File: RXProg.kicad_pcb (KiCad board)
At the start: 2 copper layers, 5 parts, among them J1 DIP-28, U1 STM32G474CETx, U2 SN74ALVC164245DL, U3 LSF0108BQ, U4 MIC5317-3.3xM5

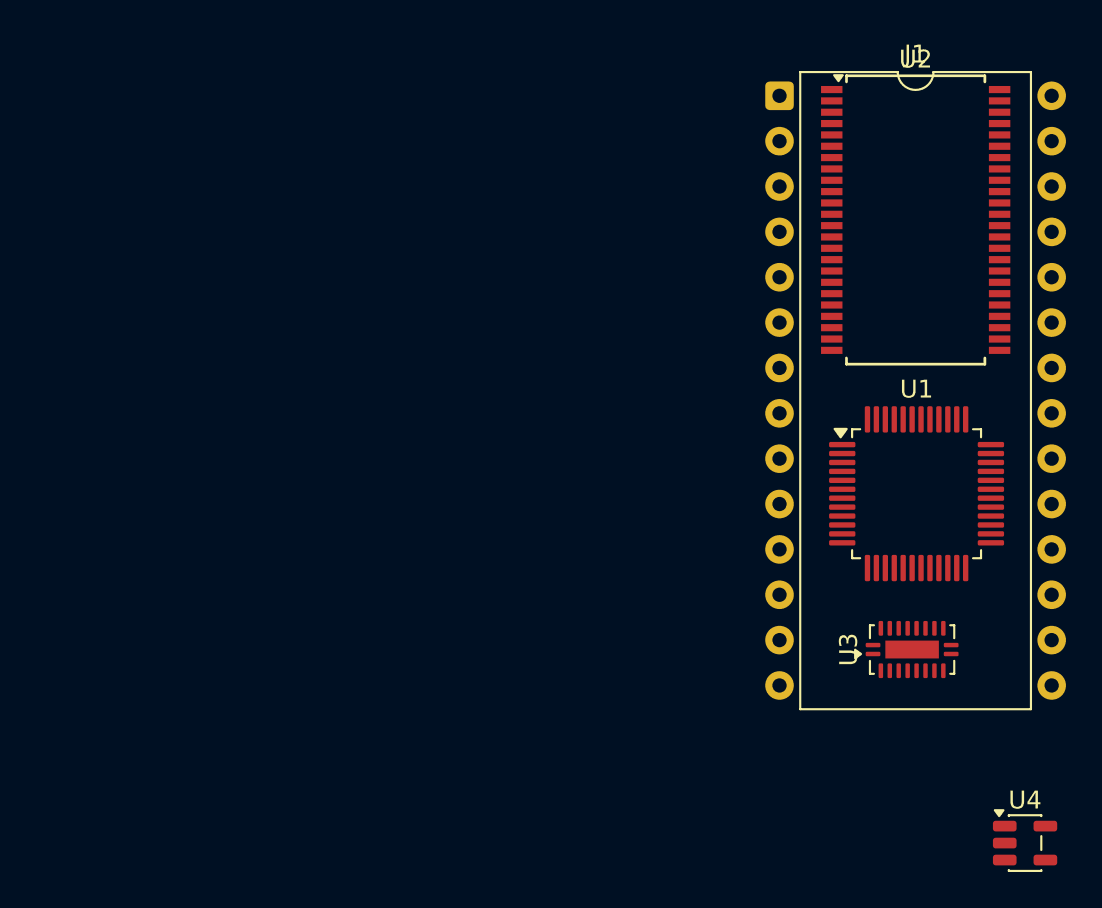
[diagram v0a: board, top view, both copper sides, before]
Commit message: Add level shifters
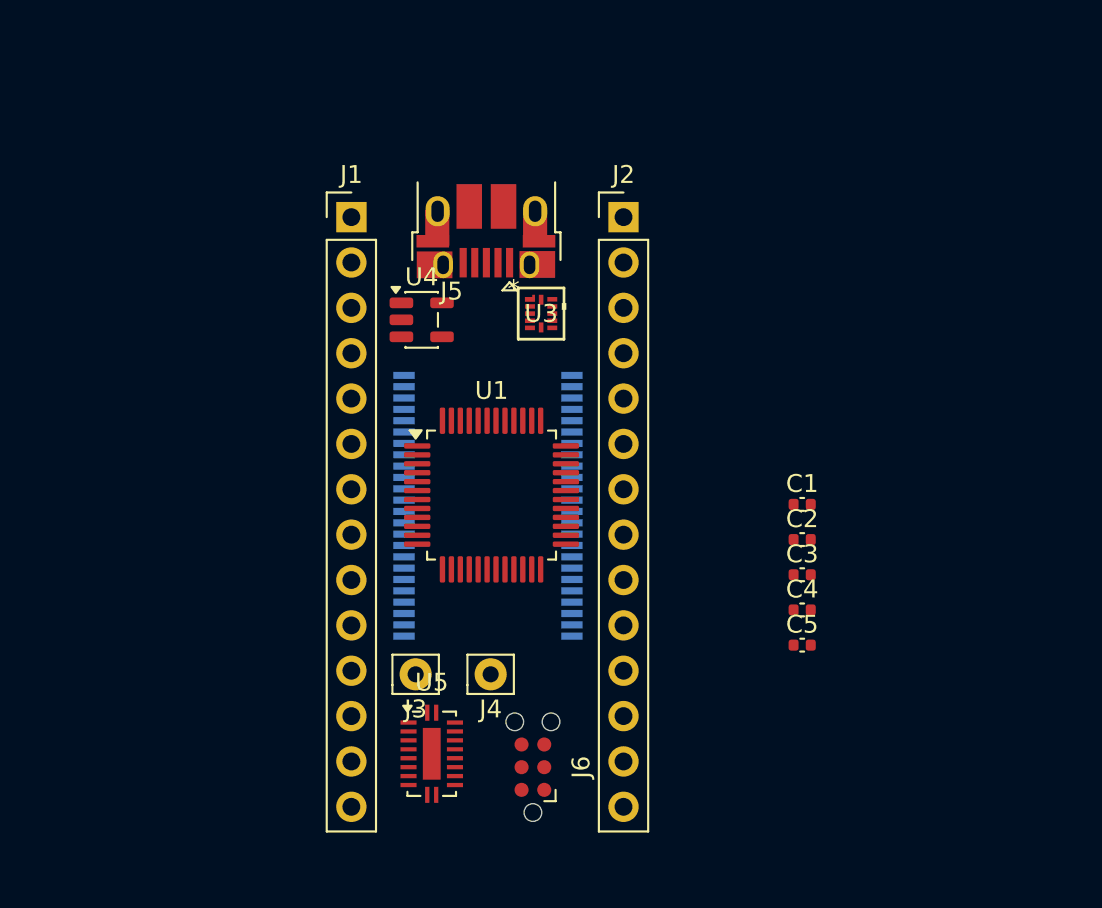
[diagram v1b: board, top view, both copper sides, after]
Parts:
- added C1: 100n, Capacitor_SMD:C_0402_1005Metric, F.Cu at (143.8, 107.7)
- added C2: 100n, Capacitor_SMD:C_0402_1005Metric, F.Cu at (143.8, 109.7)
- added C3: 100n, Capacitor_SMD:C_0402_1005Metric, F.Cu at (143.8, 111.6)
- added C4: 100n, Capacitor_SMD:C_0402_1005Metric, F.Cu at (143.8, 113.6)
- added C5: 100n, Capacitor_SMD:C_0402_1005Metric, F.Cu at (143.8, 115.6)
- added J2: Conn_01x14, Connector_PinHeader_2.54mm:PinHeader_1x14_P2.54mm_Vertical, F.Cu at (133.8, 91.6)
- added J3: Pin, Connector_Pin:Pin_D0.9mm_L10.0mm_W2.4mm_FlatFork, F.Cu at (122.2, 117.2)
- added J4: Pin, Connector_Pin:Pin_D0.9mm_L10.0mm_W2.4mm_FlatFork, F.Cu at (126.4, 117.2)
- added J5: USB_B_Micro, Connector_USB:USB_Micro-B_Amphenol_10103594-0001LF_Horizontal, F.Cu at (126.1, 92.4)
- added J6: Conn_ARM_SWD_TagConnect_TC2030-NL, Connector:Tag-Connect_TC2030-IDC-NL_2x03_P1.27mm_Vertical, F.Cu at (128.8, 122.4)
- added U5: FXMA108, Package_DFN_QFN:WQFN-20-1EP_2.5x4.5mm_P0.5mm_EP1x2.9mm, F.Cu at (123.1, 121.7)
- J1: value DIP-28 -> Conn_01x14; footprint Package_DIP:DIP-28_W15.24mm -> Connector_PinHeader_2.54mm:PinHeader_1x14_P2.54mm_Vertical
- U2: moved to B.Cu
- U3: value LSF0108BQ -> TXU0104RUTR; footprint Package_DFN_QFN:DHVQFN-20-1EP_2.5x4.5mm_P0.5mm_EP1x3mm -> footprints:QFN_04RUTR_TEX
- moved U4 44.7 mm to (122.5, 97.3)
- moved U2 28.8 mm to (126.2, 107.8), turned to 180 degrees
- moved U3 28.0 mm to (129.2, 97.0), turned to 0 degrees
- moved J1 24.9 mm to (118.6, 91.6)
- moved U1 23.8 mm to (126.5, 107.2)
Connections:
- U1 pad 1: unconnected-(U1-VBAT-Pad1) -> +3V3
- U1 pad 10: unconnected-(U1-PA2-Pad10) -> Net-(U1-PA2)
- U1 pad 11: unconnected-(U1-PA3-Pad11) -> Net-(U1-PA3)
- U1 pad 12: unconnected-(U1-PA4-Pad12) -> Net-(U1-PA4)
- U1 pad 13: unconnected-(U1-PA5-Pad13) -> Net-(U1-PA5)
- U1 pad 14: unconnected-(U1-PA6-Pad14) -> Net-(U1-PA6)
- U1 pad 15: unconnected-(U1-PA7-Pad15) -> Net-(U1-PA7)
- U1 pad 16: A0 -> Net-(U1-PB0)
- U1 pad 17: A1 -> Net-(U1-PB1)
- U1 pad 18: A2 -> Net-(U1-PB2)
- U1 pad 19: unconnected-(U1-VSSA-Pad19) -> GND
- U1 pad 2: unconnected-(U1-PC13-Pad2) -> Net-(U1-PC13)
- U1 pad 20: unconnected-(U1-VREF+-Pad20) -> +3V3
- U1 pad 21: unconnected-(U1-VDDA-Pad21) -> +3V3
- U1 pad 22: A10 -> Net-(U1-PB10)
- U1 pad 23: Net-(U1-VSS-Pad23) -> GND
- U1 pad 24: unconnected-(U1-VDD-Pad24) -> +3V3
- U1 pad 25: ~{WE}/A11 -> Net-(U1-PB11)
- U1 pad 26: /A12 -> Net-(U1-PB12)
- U1 pad 27: unconnected-(U1-PB13-Pad27) -> Net-(U1-PB13)
- U1 pad 28: unconnected-(U1-PB14-Pad28) -> Net-(U1-PB14)
- U1 pad 29: unconnected-(U1-PB15-Pad29) -> Net-(U1-PB15)
- U1 pad 3: unconnected-(U1-PC14-Pad3) -> Net-(U1-PC14)
- U1 pad 30: unconnected-(U1-PA8-Pad30) -> Net-(U1-PA8)
- U1 pad 31: unconnected-(U1-PA9-Pad31) -> ~{ADDR_OE}
- U1 pad 33: unconnected-(U1-PA11-Pad33) -> Net-(J5-D-)
- U1 pad 34: unconnected-(U1-PA12-Pad34) -> Net-(J5-D+)
- U1 pad 35: Net-(U1-VSS-Pad23) -> GND
- U1 pad 36: unconnected-(U1-VDD-Pad36) -> +3V3
- U1 pad 4: unconnected-(U1-PC15-Pad4) -> Net-(U1-PC15)
- U1 pad 40: A3 -> Net-(U1-PB3)
- U1 pad 41: A4 -> Net-(U1-PB4)
- U1 pad 42: A5 -> Net-(U1-PB5)
- U1 pad 43: A6 -> Net-(U1-PB6)
- U1 pad 44: A7 -> Net-(U1-PB7)
- U1 pad 45: A8 -> Net-(U1-PB8)
- U1 pad 46: A9 -> Net-(U1-PB9)
- U1 pad 47: Net-(U1-VSS-Pad23) -> GND
- U1 pad 48: unconnected-(U1-VDD-Pad48) -> +3V3
- U1 pad 8: unconnected-(U1-PA0-Pad8) -> Net-(U1-PA0)
- U1 pad 9: unconnected-(U1-PA1-Pad9) -> Net-(U1-PA1)
- U2 pad 1: unconnected-(U2-1DIR-Pad1) -> GND
- U2 pad 10: Net-(U2-GND-Pad10) -> GND
- U2 pad 11: unconnected-(U2-1B6-Pad11) -> A6
- U2 pad 12: unconnected-(U2-1B7-Pad12) -> A7
- U2 pad 13: unconnected-(U2-2B0-Pad13) -> A8
- U2 pad 14: unconnected-(U2-2B1-Pad14) -> A9
- U2 pad 15: Net-(U2-GND-Pad10) -> GND
- U2 pad 16: unconnected-(U2-2B2-Pad16) -> A10
- U2 pad 17: unconnected-(U2-2B3-Pad17) -> ~{WE}/A11
- U2 pad 18: Net-(U2-V_{CC(B)}-Pad18) -> /VBAT
- U2 pad 19: unconnected-(U2-2B4-Pad19) -> /A12
- U2 pad 2: unconnected-(U2-1B0-Pad2) -> A0
- U2 pad 20: unconnected-(U2-2B5-Pad20) -> ~{CS1}
- U2 pad 21: Net-(U2-GND-Pad10) -> GND
- U2 pad 22: unconnected-(U2-2B6-Pad22) -> ~{CS2}
- U2 pad 23: unconnected-(U2-2B7-Pad23) -> ~{CS3}
- U2 pad 24: unconnected-(U2-2DIR-Pad24) -> GND
- U2 pad 25: unconnected-(U2-2~{OE}-Pad25) -> ~{ADDR_OE}
- U2 pad 26: unconnected-(U2-2A7-Pad26) -> Net-(U1-PB15)
- U2 pad 27: unconnected-(U2-2A6-Pad27) -> Net-(U1-PB14)
- U2 pad 28: Net-(U2-GND-Pad10) -> GND
- U2 pad 29: unconnected-(U2-2A5-Pad29) -> Net-(U1-PB13)
- U2 pad 3: unconnected-(U2-1B1-Pad3) -> A1
- U2 pad 30: unconnected-(U2-2A4-Pad30) -> Net-(U1-PB12)
- U2 pad 31: Net-(U2-V_{CC(A)}-Pad31) -> +3V3
- U2 pad 32: unconnected-(U2-2A3-Pad32) -> Net-(U1-PB11)
- U2 pad 33: unconnected-(U2-2A2-Pad33) -> Net-(U1-PB10)
- U2 pad 34: Net-(U2-GND-Pad10) -> GND
- U2 pad 35: unconnected-(U2-2A1-Pad35) -> Net-(U1-PB9)
- U2 pad 36: unconnected-(U2-2A0-Pad36) -> Net-(U1-PB8)
- U2 pad 37: unconnected-(U2-1A7-Pad37) -> Net-(U1-PB7)
- U2 pad 38: unconnected-(U2-1A6-Pad38) -> Net-(U1-PB6)
- U2 pad 39: Net-(U2-GND-Pad10) -> GND
- U2 pad 4: Net-(U2-GND-Pad10) -> GND
- U2 pad 40: unconnected-(U2-1A5-Pad40) -> Net-(U1-PB5)
- U2 pad 41: unconnected-(U2-1A4-Pad41) -> Net-(U1-PB4)
- U2 pad 42: Net-(U2-V_{CC(A)}-Pad31) -> +3V3
- U2 pad 43: unconnected-(U2-1A3-Pad43) -> Net-(U1-PB3)
- U2 pad 44: unconnected-(U2-1A2-Pad44) -> Net-(U1-PB2)
- U2 pad 45: Net-(U2-GND-Pad10) -> GND
- U2 pad 46: unconnected-(U2-1A1-Pad46) -> Net-(U1-PB1)
- U2 pad 47: unconnected-(U2-1A0-Pad47) -> Net-(U1-PB0)
- U2 pad 48: unconnected-(U2-1~{OE}-Pad48) -> ~{ADDR_OE}
- U2 pad 5: unconnected-(U2-1B2-Pad5) -> A2
- U2 pad 6: unconnected-(U2-1B3-Pad6) -> A3
- U2 pad 7: Net-(U2-V_{CC(B)}-Pad18) -> /VBAT
- U2 pad 8: unconnected-(U2-1B4-Pad8) -> A4
- U2 pad 9: unconnected-(U2-1B5-Pad9) -> A5
- U3 pad 1: unconnected-(U3-GND-Pad1) -> /VBAT
- U3 pad 10: unconnected-(U3-A8-Pad10) -> Net-(U1-PC13)
- U3 pad 11: unconnected-(U3-B8-Pad11) -> +3V3
- U3 pad 12: unconnected-(U3-B7-Pad12) -> +3V3
- U3 pad 2: unconnected-(U3-RefA-Pad2) -> VBAT/~{RES}
- U3 pad 3: unconnected-(U3-A1-Pad3) -> RES/~{OE}
- U3 pad 4: unconnected-(U3-A2-Pad4) -> /~{WE}
- U3 pad 6: unconnected-(U3-A4-Pad6) -> GND
- U3 pad 8: unconnected-(U3-A6-Pad8) -> Net-(U1-PC15)
- U3 pad 9: unconnected-(U3-A7-Pad9) -> Net-(U1-PC14)
- U4 pad 1: unconnected-(U4-VIN-Pad1) -> /VBAT
- U4 pad 2: unconnected-(U4-GND-Pad2) -> GND
- U4 pad 3: unconnected-(U4-EN-Pad3) -> /VBAT
- U4 pad 5: unconnected-(U4-VOUT-Pad5) -> +3V3

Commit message: Add
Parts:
- added C6: 100n, Capacitor_SMD:C_0402_1005Metric, F.Cu at (144.2, 119.5)
- added C7: 10u, Capacitor_SMD:C_0402_1005Metric, F.Cu at (144.2, 121.5)
- added C8: 10u, Capacitor_SMD:C_0402_1005Metric, F.Cu at (144.2, 123.4)
- added D1: CD214A-B140LR, footprints:CD214A, F.Cu at (126.2, 98.5)
- added U6: FM25V02A, footprints:DFN-8_4x4.5mm_P0.95mm, B.Cu at (123.2, 121.8)
- J6: value Conn_ARM_SWD_TagConnect_TC2030-NL -> SWD
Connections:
- J6 pad 1: unconnected-(J6-VCC-Pad1) -> +3V3
- J6 pad 2: unconnected-(J6-SWDIO-Pad2) -> Net-(J6-SWDIO)
- J6 pad 3: unconnected-(J6-~{RESET}-Pad3) -> ~{NRST}
- J6 pad 4: unconnected-(J6-SWCLK-Pad4) -> Net-(J6-SWCLK)
- J6 pad 5: unconnected-(J6-GND-Pad5) -> GND
- U1 pad 32: unconnected-(U1-PA10-Pad32) -> ~{FRAM_CS}
- U1 pad 37: unconnected-(U1-PA13-Pad37) -> Net-(J6-SWDIO)
- U1 pad 38: unconnected-(U1-PA14-Pad38) -> Net-(J6-SWCLK)
- U1 pad 7: unconnected-(U1-PG10-Pad7) -> ~{NRST}

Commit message: Start routing
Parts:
- removed U6: FM25V02A, footprints:DFN-8_4x4.5mm_P0.95mm
- added C10: 100n, Capacitor_SMD:C_0201_0603Metric, F.Cu at (147.7, 114.8)
- added C11: 100n, Capacitor_SMD:C_0201_0603Metric, F.Cu at (147.7, 116.8)
- added C9: 100n, Capacitor_SMD:C_0201_0603Metric, F.Cu at (126.8, 96.7)
- added JP1: RX5_Select, Jumper:SolderJumper-2_P1.3mm_Open_RoundedPad1.0x1.5mm, F.Cu at (107.1, 99.3)
- C1, C2, C3, C4, C5, C6: footprint Capacitor_SMD:C_0402_1005Metric -> Capacitor_SMD:C_0201_0603Metric
- C7: value 10u -> 1u; footprint Capacitor_SMD:C_0402_1005Metric -> Capacitor_SMD:C_0201_0603Metric; moved to B.Cu
- C8: value 10u -> 1u; footprint Capacitor_SMD:C_0402_1005Metric -> Capacitor_SMD:C_0201_0603Metric
- D1: value CD214A-B140LR -> RB531SM-30T2R; footprint footprints:CD214A -> Diode_SMD:D_SOD-523
- J3, J4: footprint Connector_Pin:Pin_D0.9mm_L10.0mm_W2.4mm_FlatFork -> footprints:Pin
- moved C8 35.4 mm to (127.2, 92.4), turned to 90 degrees
- moved C7 31.6 mm to (131.2, 92.6), turned to 90 degrees
- moved J5 31.1 mm to (126.2, 123.5), turned to 0 degrees
- moved J6 27.0 mm to (102.4, 116.3)
- moved C6 26.8 mm to (129.0, 97.4), turned to 180 degrees
- moved U5 14.6 mm to (109.0, 125.1)
- moved J3 12.9 mm to (109.8, 113.8)
- moved J4 12.9 mm to (114.0, 113.8)
- moved U4 9.14 mm to (129.8, 91.8), turned to 180 degrees
- moved D1 4.97 mm to (130.8, 96.5)
- moved U3 1.71 mm to (128.6, 95.4), turned to 180 degrees
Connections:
- net Net-(J5-D+) renamed /D_+
- net Net-(J5-D-) renamed /D_-
- C6 pad 1: +3V3 -> /VBAT
- U1 pad 39: unconnected-(U1-PA15-Pad39) -> Net-(JP1-B)
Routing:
- net RES/~{OE}: track 0.00 -> 14.7 mm, vias 0 -> 1
- net /VBAT: track 0.00 -> 7.98 mm, vias 0 -> 2
- net GND: track 0.00 -> 5.77 mm, vias 0 -> 4
- net VBAT/~{RES}: track 0.00 -> 4.95 mm
- net /~{WE}: track 0.00 -> 4.95 mm
- net +3V3: track 0.00 -> 1.87 mm
- added copper zone on F.Cu, net +3V3
- added copper zone on In1.Cu, net GND
- added copper zone on In2.Cu, net GND
- added copper zone on B.Cu, net /VBAT
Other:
- board outline added: 18.8 x 36.6 mm
- copper layers 2 -> 4

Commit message: Continue
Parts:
- moved J6 30.1 mm to (122.6, 94.0), turned to -90 degrees
- moved JP1 19.6 mm to (126.0, 94.2), turned to -90 degrees
- moved C8 0.66 mm to (127.2, 91.7), turned to -90 degrees
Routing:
- net GND: track 5.77 -> 8.75 mm, vias 4 -> 5
- net /VBAT: track 7.98 -> 8.80 mm, vias 2 -> 3
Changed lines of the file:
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@@
 		(capping no)
 		(filling no)
-		(zone_defaults)
 		(pcbplotparams
 			(layerselection 0x00000000_00000000_55555555_5755f5ff)
@@
 	(footprint "Connector:Tag-Connect_TC2030-IDC-NL_2x03_P1.27mm_Vertical"
 		(layer "F.Cu")
-		(at 102.435 116.33 90)
+		(at 122.615 93.98 -90)
 		(descr "Tag-Connect programming header; http://www.tag-connect.com/Materials/TC2030-IDC-NL.pdf")
 		(tags "tag connect programming header pogo pins")
@@
 		)
 		(property "Datasheet" "https://www.tag-connect.com/wp-content/uploads/bsk-pdf-manager/TC2030-CTX_1.pdf"
-			(at 0 0 90)
+			(at 0 0 270)
 			(unlocked yes)
 			(layer "F.Fab")
@@
 		)
 		(property "Description" "Tag-Connect ARM Cortex SWD JTAG connector, 6 pin, no legs"
-			(at 0 0 90)
+			(at 0 0 270)
 			(unlocked yes)
 			(layer "F.Fab")
@@
 		(duplicate_pad_numbers_are_jumpers no)
 		(fp_line
-			(start -1.27 1.27)
-			(end -1.905 1.27)
+			(start -1.905 1.27)
+			(end -1.905 0.635)
 			(stroke
 				(width 0.12)
@@
 		)
 		(fp_line
-			(start -1.905 1.27)
-			(end -1.905 0.635)
+			(start -1.27 1.27)
+			(end -1.905 1.27)
 			(stroke
 				(width 0.12)
@@
 		)
 		(fp_line
-			(start 3.5 -2)
-			(end 3.5 2)
+			(start -3.5 2)
+			(end -3.5 -2)
 			(stroke
 				(width 0.05)
@@
 		)
 		(fp_line
-			(start -3.5 -2)
-			(end 3.5 -2)
+			(start 3.5 2)
+			(end -3.5 2)
 			(stroke
 				(width 0.05)
@@
 		)
 		(fp_line
-			(start 3.5 2)
-			(end -3.5 2)
+			(start -3.5 -2)
+			(end 3.5 -2)
 			(stroke
 				(width 0.05)
@@
 		)
 		(fp_line
-			(start -3.5 2)
-			(end -3.5 -2)
+			(start 3.5 -2)
+			(end 3.5 2)
 			(stroke
 				(width 0.05)
@@
 		)
 		(pad "" np_thru_hole circle
-			(at -2.54 0 90)
+			(at -2.54 0 270)
 			(size 0.9906 0.9906)
 			(drill 0.9906)
@@
 		)
 		(pad "" np_thru_hole circle
-			(at 2.54 -1.016 90)
+			(at 2.54 -1.016 270)
 			(size 0.9906 0.9906)
 			(drill 0.9906)
@@
 		)
 		(pad "" np_thru_hole circle
-			(at 2.54 1.016 90)
+			(at 2.54 1.016 270)
 			(size 0.9906 0.9906)
 			(drill 0.9906)
@@
 		)
 		(pad "1" connect circle
-			(at -1.27 0.635 90)
+			(at -1.27 0.635 270)
 			(size 0.7874 0.7874)
 			(layers "F.Cu" "F.Mask")
@@
 		)
 		(pad "2" connect circle
-			(at -1.27 -0.635 90)
+			(at -1.27 -0.635 270)
 			(size 0.7874 0.7874)
 			(layers "F.Cu" "F.Mask")
@@
 		)
 		(pad "3" connect circle
-			(at 0 0.635 90)
+			(at 0 0.635 270)
 			(size 0.7874 0.7874)
 			(layers "F.Cu" "F.Mask")
@@
 		)
 		(pad "4" connect circle
-			(at 0 -0.635 90)
+			(at 0 -0.635 270)
 			(size 0.7874 0.7874)
 			(layers "F.Cu" "F.Mask")
@@
 		)
 		(pad "5" connect circle
-			(at 1.27 0.635 90)
+			(at 1.27 0.635 270)
 			(size 0.7874 0.7874)
 			(layers "F.Cu" "F.Mask")
@@
 		)
 		(pad "6" connect circle
-			(at 1.27 -0.635 90)
+			(at 1.27 -0.635 270)
 			(size 0.7874 0.7874)
 			(layers "F.Cu" "F.Mask")
@@
 			(polygon
 				(pts
-					(xy 101.8 115.06) (xy 101.8 117.6) (xy 103.07 117.6) (xy 103.07 115.06)
+					(xy 123.25 95.25) (xy 123.25 92.71) (xy 121.98 92.71) (xy 121.98 95.25)
 				)
 			)
@@
 	(footprint "Jumper:SolderJumper-2_P1.3mm_Open_RoundedPad1.0x1.5mm"
 		(layer "F.Cu")
-		(at 107.075 99.275)
+		(at 126 94.2 -90)
 		(descr "SMD Solder Jumper, 1x1.5mm, rounded Pads, 0.3mm gap, open")
 		(tags "solder jumper open")
 		(property "Reference" "JP1"
-			(at 0 -1.8 0)
+			(at 0 -1.8 90)
 			(layer "F.SilkS")
+			(hide yes)
 			(effects
 				(font
@@
 		)
 		(property "Value" "RX5_Select"
-			(at 0 1.9 0)
+			(at 0 1.9 90)
 			(layer "F.Fab")
+			(hide yes)
 			(effects
 				(font
@@
 		)
 		(property "Datasheet" ""
-			(at 0 0 0)
+			(at 0 0 270)
 			(unlocked yes)
 			(layer "F.Fab")
@@
 		)
 		(property "Description" "Solder Jumper, 2-pole, open"
-			(at 0 0 0)
+			(at 0 0 270)
 			(unlocked yes)
 			(layer "F.Fab")
@@
 		)
 		(fp_line
-			(start -1.4 0.3)
-			(end -1.4 -0.3)
+			(start 0.7 1)
+			(end -0.7 1)
 			(stroke
 				(width 0.12)
@@
 		)
 		(fp_line
-			(start -0.7 -1)
-			(end 0.7 -1)
+			(start -1.4 0.3)
+			(end -1.4 -0.3)
 			(stroke
 				(width 0.12)
@@
 		)
 		(fp_line
-			(start 0.7 1)
-			(end -0.7 1)
+			(start 1.4 -0.3)
+			(end 1.4 0.3)
 			(stroke
 				(width 0.12)
@@
 		)
 		(fp_line
-			(start 1.4 -0.3)
-			(end 1.4 0.3)
+			(start -0.7 -1)
+			(end 0.7 -1)
 			(stroke
 				(width 0.12)
@@
 		)
 		(fp_arc
-			(start -1.4 -0.3)
-			(mid -1.194975 -0.794975)
-			(end -0.7 -1)
+			(start -0.7 1)
+			(mid -1.194975 0.794975)
+			(end -1.4 0.3)
 			(stroke
 				(width 0.12)
@@
 		)
 		(fp_arc
-			(start -0.7 1)
-			(mid -1.194975 0.794975)
-			(end -1.4 0.3)
+			(start 1.4 0.3)
+			(mid 1.194975 0.794975)
+			(end 0.7 1)
 			(stroke
 				(width 0.12)
@@
 		)
 		(fp_arc
-			(start 0.7 -1)
-			(mid 1.194975 -0.794975)
-			(end 1.4 -0.3)
+			(start -1.4 -0.3)
+			(mid -1.194975 -0.794975)
+			(end -0.7 -1)
 			(stroke
 				(width 0.12)
@@
 		)
 		(fp_arc
-			(start 1.4 0.3)
-			(mid 1.194975 0.794975)
-			(end 0.7 1)
+			(start 0.7 -1)
+			(mid 1.194975 -0.794975)
+			(end 1.4 -0.3)
 			(stroke
 				(width 0.12)
@@
 		)
 		(fp_line
-			(start -1.65 -1.25)
+			(start 1.65 1.25)
 			(end -1.65 1.25)
 			(stroke
@@
 		)
 		(fp_line
-			(start -1.65 -1.25)
+			(start 1.65 1.25)
 			(end 1.65 -1.25)
 			(stroke
@@
 		)
 		(fp_line
-			(start 1.65 1.25)
+			(start -1.65 -1.25)
 			(end -1.65 1.25)
 			(stroke
@@
 		)
 		(fp_line
-			(start 1.65 1.25)
+			(start -1.65 -1.25)
 			(end 1.65 -1.25)
 			(stroke
@@
 		)
 		(pad "1" smd custom
-			(at -0.65 0)
+			(at -0.65 0 270)
 			(size 1 0.5)
 			(layers "F.Cu" "F.Mask")
@@
 		)
 		(pad "2" smd custom
-			(at 0.65 0)
+			(at 0.65 0 270)
 			(size 1 0.5)
 			(layers "F.Cu" "F.Mask")
@@
 	(footprint "Capacitor_SMD:C_0201_0603Metric"
 		(layer "F.Cu")
-		(at 127.2 92.4 90)
+		(at 127.2 91.745 -90)
 		(descr "Capacitor SMD 0201 (0603 Metric), square (rectangular) end terminal, IPC-7351 nominal, (Body size source: https://www.vishay.com/docs/20052/crcw0201e3.pdf)")
 		(tags "capacitor")
@@
 		)
 		(pad "" smd roundrect
-			(at -0.345 0 90)
+			(at -0.345 0 270)
 			(size 0.318 0.36)
 			(layers "F.Paste")
@@
 		)
 		(pad "" smd roundrect
-			(at 0.345 0 90)
+			(at 0.345 0 270)
 			(size 0.318 0.36)
 			(layers "F.Paste")
@@
 		)
 		(pad "1" smd roundrect
-			(at -0.32 0 90)
+			(at -0.32 0 270)
 			(size 0.46 0.4)
 			(layers "F.Cu" "F.Mask")
@@
 		)
 		(pad "2" smd roundrect
-			(at 0.32 0 90)
+			(at 0.32 0 270)
 			(size 0.46 0.4)
 			(layers "F.Cu" "F.Mask")
@@
 	)
 	(segment
+		(start 126 93.55)
+		(end 126 93.265)
+		(width 0.2)
+		(layer "F.Cu")
+		(net "GND")
+	)
+	(segment
 		(start 126.825 96.975)
 		(end 127.6 96.975)
@@
 	)
 	(segment
+		(start 121.05 95.25)
+		(end 121 95.2)
+		(width 0.2)
+		(layer "F.Cu")
+		(net "GND")
+	)
+	(segment
 		(start 128.625 94.625)
 		(end 128.625 94)
@@
 	)
 	(segment
+		(start 126 93.265)
+		(end 127.2 92.065)
+		(width 0.2)
+		(layer "F.Cu")
+		(net "GND")
+	)
+	(segment
 		(start 130.9375 91.8)
 		(end 131.502042 91.8)
@@
 		(net "GND")
 	)
+	(segment
+		(start 121.98 95.25)
+		(end 121.05 95.25)
+		(width 0.2)
+		(layer "F.Cu")
+		(net "GND")
+	)
 	(via
 		(at 128.625 94)
@@
 	)
 	(via
+		(at 121 95.2)
+		(size 0.6)
+		(drill 0.3)
+		(layers "F.Cu" "B.Cu")
+		(net "GND")
+	)
+	(via
 		(at 128 91.8)
 		(size 0.6)
@@
 	)
 	(segment
+		(start 130.8 97.2)
+		(end 130.8 97.95)
+		(width 0.2)
+		(layer "F.Cu")
+		(net "{slash}VBAT")
+	)
+	(segment
+		(start 130.8 97.95)
+		(end 130.75 98)
+		(width 0.2)
+		(layer "F.Cu")
+		(net "{slash}VBAT")
+	)
+	(segment
 		(start 131.2 93.0125)
 		(end 130.9375 92.75)
@@
 		(net "{slash}VBAT")
 	)
+	(via
+		(at 130.75 98)
+		(size 0.6)
+		(drill 0.3)
+		(layers "F.Cu" "B.Cu")
+		(net "{slash}VBAT")
+	)

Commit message: Finished routing
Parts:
- added C12: 100n, Capacitor_SMD:C_0201_0603Metric, F.Cu at (127.0, 116.8)
- moved C10 28.3 mm to (122.8, 101.4), turned to 90 degrees
- moved C4 22.3 mm to (121.7, 111.6), turned to 180 degrees
- moved J3 21.5 mm to (130.8, 118.6)
- moved C5 17.1 mm to (127.0, 118.5), turned to -90 degrees
- moved J4 17.0 mm to (130.8, 116.4)
- moved C11 16.9 mm to (131.6, 111.7), turned to -90 degrees
- moved U5 16.2 mm to (123.5, 117.9), turned to -90 degrees
- moved C2 15.1 mm to (130.4, 102.8), turned to 90 degrees
- moved C3 13.9 mm to (130.0, 112.1), turned to -90 degrees
- moved C1 13.4 mm to (131.2, 103.3), turned to 90 degrees
- moved JP1 6.30 mm to (126.0, 100.5), turned to 0 degrees
- moved U2 0.76 mm to (126.2, 107.0), turned to 0 degrees
- moved C9 0.36 mm to (127.2, 96.7)
- moved C6 0.35 mm to (129.3, 97.4)
- moved D1 0.35 mm to (131.2, 96.5)
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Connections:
- U1 pad 32: ~{FRAM_CS} -> unconnected-(U1-PA10-Pad32)
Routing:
- net GND: track 8.75 -> 46.5 mm, vias 5 -> 19
- net ~{CS1}: track 0.00 -> 28.3 mm, vias 0 -> 1
- net A8: track 0.00 -> 27.5 mm, vias 0 -> 1
- net Net-(J6-SWCLK): track 0.00 -> 24.2 mm, vias 0 -> 2
- net Net-(J6-SWDIO): track 0.00 -> 23.9 mm, vias 0 -> 2
- net ~{ADDR_OE}: track 0.00 -> 23.2 mm, vias 0 -> 1
- net ~{CS2}: track 0.00 -> 22.1 mm, vias 0 -> 1
- net ~{CS3}: track 0.00 -> 21.2 mm, vias 0 -> 1
- net /VBAT: track 8.80 -> 29.6 mm, vias 3 -> 8
- net +3V3: track 1.87 -> 20.9 mm, vias 0 -> 6
- net A9: track 0.00 -> 17.5 mm, vias 0 -> 1
- net A10: track 0.00 -> 17.0 mm, vias 0 -> 1
- net ~{NRST}: track 0.00 -> 16.6 mm, vias 0 -> 2
- net Net-(U1-PB0): track 0.00 -> 16.0 mm, vias 0 -> 1
- net Net-(U1-PB15): track 0.00 -> 15.9 mm, vias 0 -> 1
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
